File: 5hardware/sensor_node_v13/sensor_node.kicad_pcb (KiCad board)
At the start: 2 copper layers, 24 x 46.5 mm, 39 parts, among them J1 Conn_01x08_Socket, J2 Conn_01x08_Socket, Q2 AO3401A, Q3 MMBT5551L, Q4 AO3401A, SW1 SW_Push, SW2 SW_Push, SW3 SW_Push, SW4 SW_Reed, SW5 SW_Push, SW6 SW_Push, SW7 SW_Push, U1 ESP-12F, U12 APDS-9960, U13 SHT31-DIS, U17 BH1750FVI-TR, U2 2N7002DW, U7 XC6206PxxxMR, U8 TPL5110

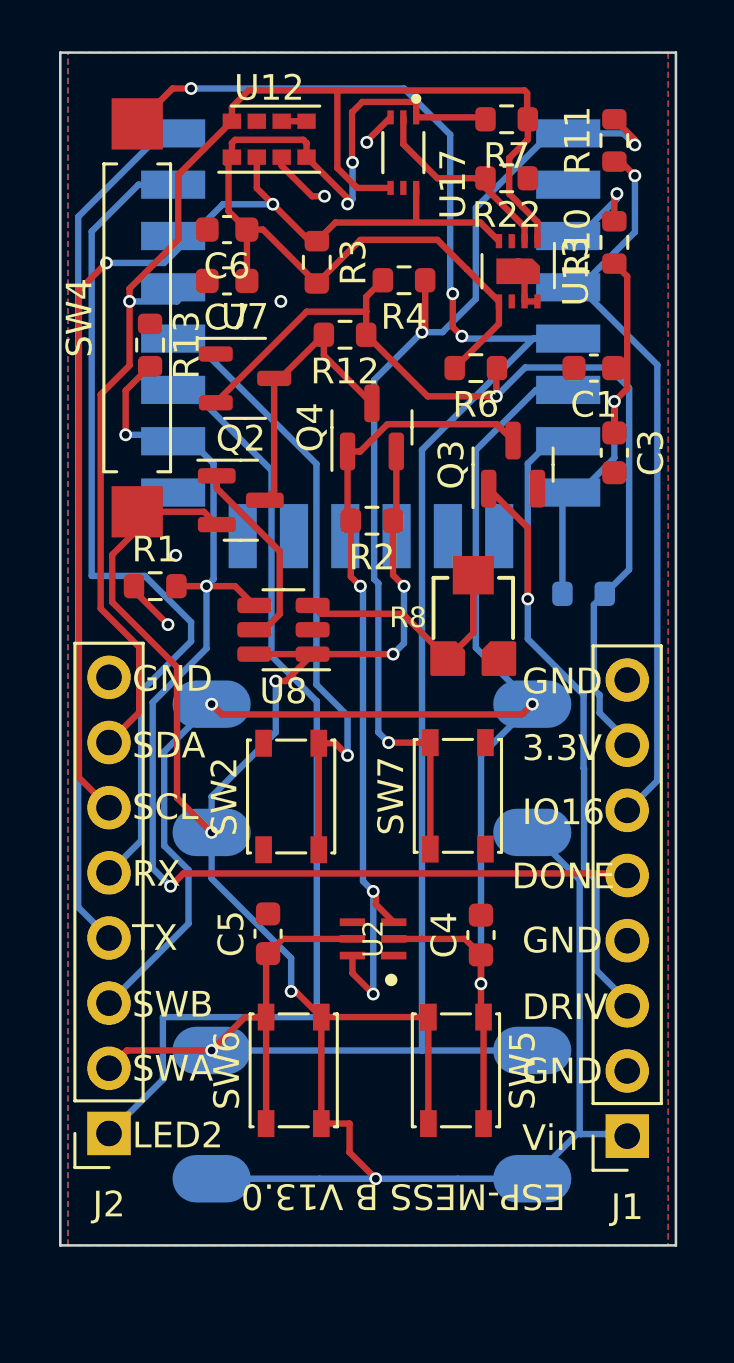
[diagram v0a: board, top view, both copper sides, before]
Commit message: update schematic.
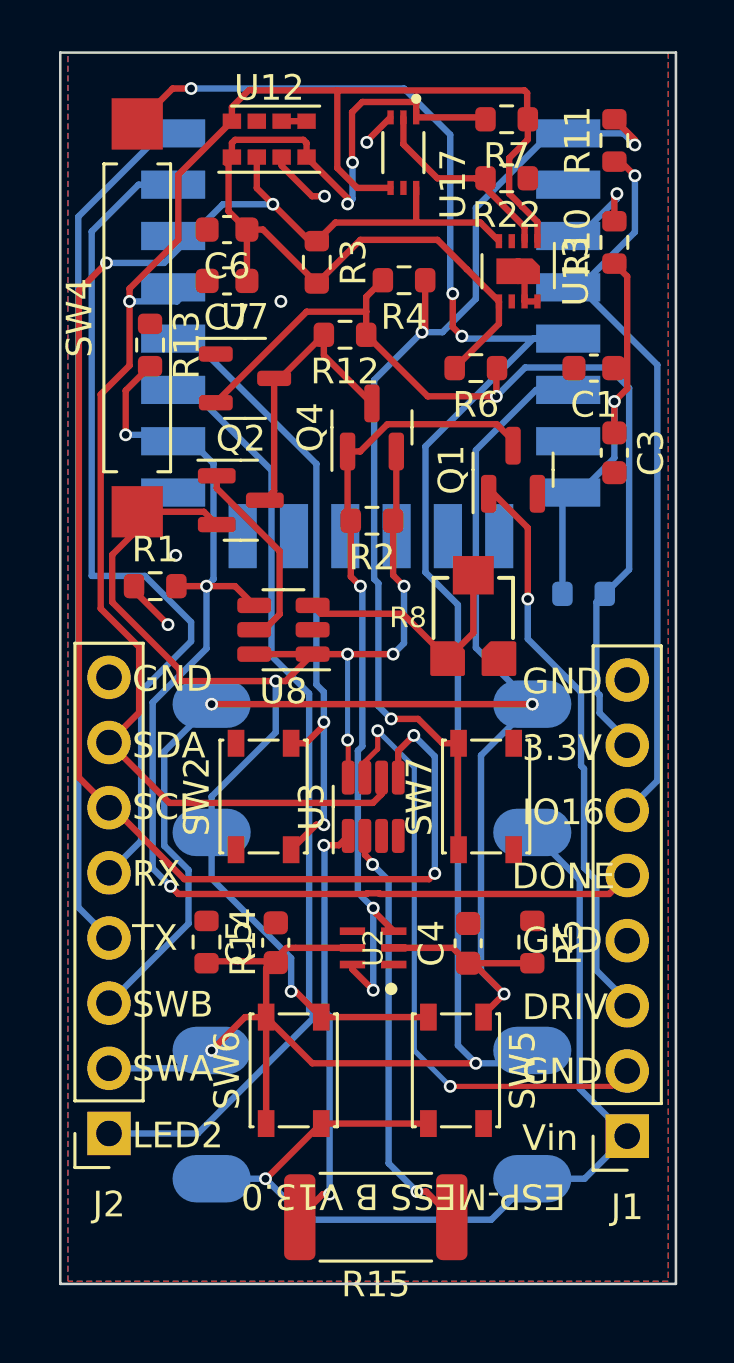
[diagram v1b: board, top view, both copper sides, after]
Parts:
- removed Q3: MMBT5551L, Package_TO_SOT_SMD:SOT-23
- added Q1: AO3400A, Package_TO_SOT_SMD:SOT-23, F.Cu at (130.3, 70.2)
- added R14: R, Resistor_SMD:R_0603_1608Metric, F.Cu at (118.4, 88.6)
- added R15: R, Resistor_SMD:R_2512_6332Metric, F.Cu at (125.0, 99.3)
- added R5: R, Resistor_SMD:R_0603_1608Metric, F.Cu at (131.1, 88.6)
- added U3: INA219AxDCN, Package_TO_SOT_SMD:SOT-23-8, F.Cu at (124.9, 83.3)
- moved SW7 1.10 mm to (129.3, 82.9)
- moved SW2 1.08 mm to (120.6, 82.9)
- moved C4 0.60 mm to (128.6, 88.6)
- moved C5 0.46 mm to (121.1, 88.6)
- moved U2 0.35 mm to (124.9, 88.8)
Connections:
- net Vin renamed Vi-
- J1 pad 2: GND -> Vi+
- R13 pad 2: DONE -> DRIVE
- U1 pad 10: DONE -> DRIVE
- U1 pad 7: DRIVE -> DONE
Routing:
- net Vi+: track 0.00 -> 24.2 mm, vias 0 -> 2
- net SCL: track 43.0 -> 64.5 mm, vias 2 -> 4
- net Net-(U3-IN-): track 0.00 -> 16.5 mm, vias 0 -> 2
- net Net-(U3-IN+): track 0.00 -> 16.3 mm, vias 0 -> 2
- net SDA: track 54.3 -> 66.7 mm
- net DRIVE: track 28.9 -> 22.4 mm
- net SW-A: track 85.0 -> 87.7 mm, vias 4 -> 5
- net LED2: track 37.9 -> 36.3 mm
- net Vi-: track 94.7 -> 93.2 mm, vias 6 -> 7
- net SW-B: track 63.6 -> 62.2 mm
- net Net-(Q1-D): track 32.4 -> 31.5 mm
- net Net-(U1-REST): track 40.0 -> 40.5 mm
- net Net-(U1-GPIO0): track 24.2 -> 24.5 mm, vias 1 -> 2
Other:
- board size 24 x 46.5 mm -> 24 x 48 mm

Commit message: updated PCB.
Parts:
- removed J1: Conn_01x08_Socket, Connector_PinSocket_2.54mm:PinSocket_1x08_P2.54mm_Vertical
- removed SW4: SW_Reed, Button_Switch_SMD:SW_SPST_REED_CT10-XXXX-G1
- removed SW5, SW6: SW_Push, Button_Switch_SMD:SW_SPST_PTS810
- added J3: Conn_01x09_Socket, Connector_PinSocket_2.54mm:PinSocket_1x09_P2.54mm_Vertical, F.Cu at (134.7, 98.8)
- added R16: 0K, Resistor_SMD:R_0402_1005Metric, F.Cu at (131.5, 97.7)
- added R17: R, Resistor_SMD:R_0603_1608Metric, F.Cu at (122.0, 74.1)
- added R18: R, Resistor_SMD:R_0603_1608Metric, F.Cu at (118.3, 72.4)
- added R19: 0K, Resistor_SMD:R_0402_1005Metric, F.Cu at (118.7, 75.6)
- added R20: 0K, Resistor_SMD:R_0402_1005Metric, F.Cu at (123.4, 76.4)
- R11, R12, R6: footprint Resistor_SMD:R_0603_1608Metric -> Resistor_SMD:R_0402_1005Metric
- R8: value EVM3ESX50B12 -> R; footprint EVM3ES:EMV3ESX50B12 -> Resistor_SMD:R_0603_1608Metric
- R9: footprint Resistor_SMD:R_0603_1608Metric -> Resistor_SMD:R_0402_1005Metric; moved to F.Cu
- moved R1 13.7 mm to (130.1, 75.7)
- moved U8 10.7 mm to (115.8, 67.3), turned to 90 degrees
- moved Q1 9.68 mm to (121.1, 67.3)
- moved R12 9.15 mm to (130.8, 70.8)
- moved Q2 8.50 mm to (118.8, 62.9), turned to -90 degrees
- moved U3 8.30 mm to (124.9, 91.6), turned to 180 degrees
- moved R8 8.06 mm to (122.0, 71.6), turned to 180 degrees
- moved U7 7.20 mm to (126.3, 63.3), turned to -90 degrees
- moved R6 6.68 mm to (130.8, 72.6)
- moved C6 5.80 mm to (115.8, 56.1)
- moved R4 5.55 mm to (129.7, 67.0), turned to 90 degrees
- moved C7 5.33 mm to (115.8, 58.7)
- moved R13 3.29 mm to (115.1, 62.2)
- moved R15 2.50 mm to (124.9, 96.8)
- moved SW7 2.44 mm to (127.9, 80.9)
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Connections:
- net Net-(Q2-D) renamed S1
- J2 pad 6: SCL -> GND
- J2 pad 7: SDA -> SCL
- J2 pad 8: GND -> SDA
- Q2 pad 2: Vi- -> S2
- Q4 pad 2: Vi- -> S2
- R2 pad 1: Vi- -> S2
- R8 pad 1: Net-(U8-DELAY/M_DRV) -> GND
- SW1 pad 1: Vi- -> S2
- SW3 pad 1: Vi- -> S2
- U8 pad 1: Vi- -> S2
- U8 pad 6: Vi- -> S2
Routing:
- net S2: track 0.00 -> 98.5 mm, vias 0 -> 7
- net Vi-: track 93.2 -> 16.2 mm, vias 7 -> 0
- net V-SENS: track 37.4 -> 74.6 mm, vias 2 -> 5
- net DRIVE: track 22.4 -> 54.7 mm, vias 1 -> 5
- net S1: track 11.0 -> 36.4 mm, vias 0 -> 1
- net SW-A: track 87.7 -> 67.0 mm, vias 5 -> 2
- net SDA: track 66.7 -> 78.9 mm, vias 1 -> 3
- net Net-(U3-IN-): track 16.5 -> 5.75 mm, vias 2 -> 0
- net Net-(U3-IN+): track 16.3 -> 8.61 mm
- net Vi+: track 24.2 -> 18.9 mm, vias 2 -> 0
- net Net-(Q1-D): track 31.5 -> 27.2 mm
- net LED2: track 36.3 -> 40.6 mm
- net IO16: track 29.4 -> 32.4 mm
- net SCL: track 64.5 -> 67.4 mm, vias 4 -> 2
- net SW-B: track 62.2 -> 64.7 mm
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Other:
- board size 24 x 48 mm -> 24.5 x 48 mm
- board text added: "ESP-MESS B V13.2"
- board text added: "S1"
- board text added: "S2"
- board text added: "Vi+"
- board text added: "Vi-"
- board text removed: "ESP-MESS B V13.0"
- board text removed: "Vin"
